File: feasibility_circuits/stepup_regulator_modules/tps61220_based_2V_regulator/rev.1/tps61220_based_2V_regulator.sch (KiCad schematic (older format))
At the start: 19 parts

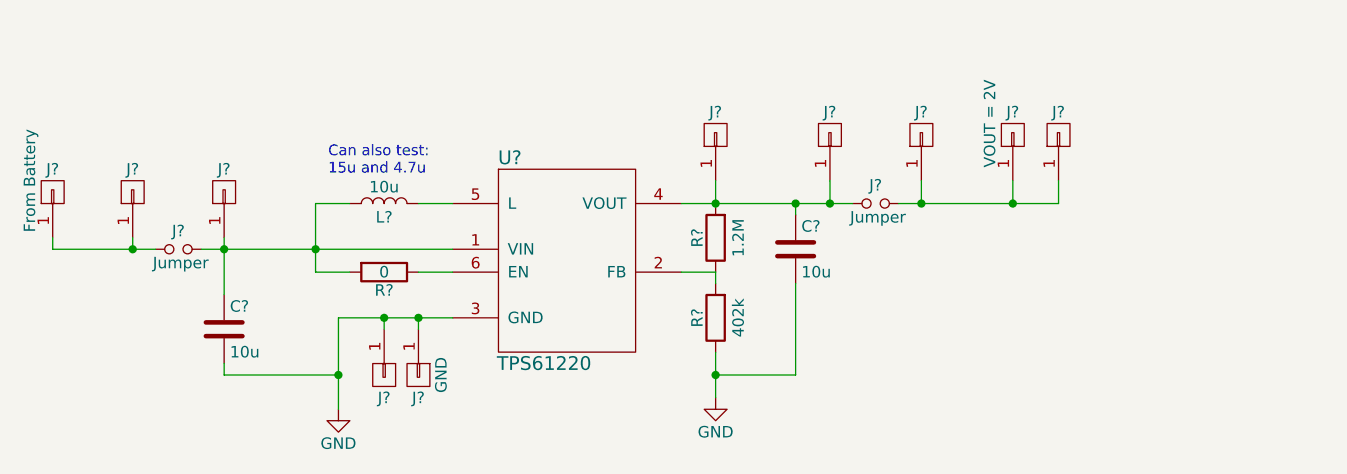
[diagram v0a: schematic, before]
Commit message: Finished layout of the TPS61220 regulator board
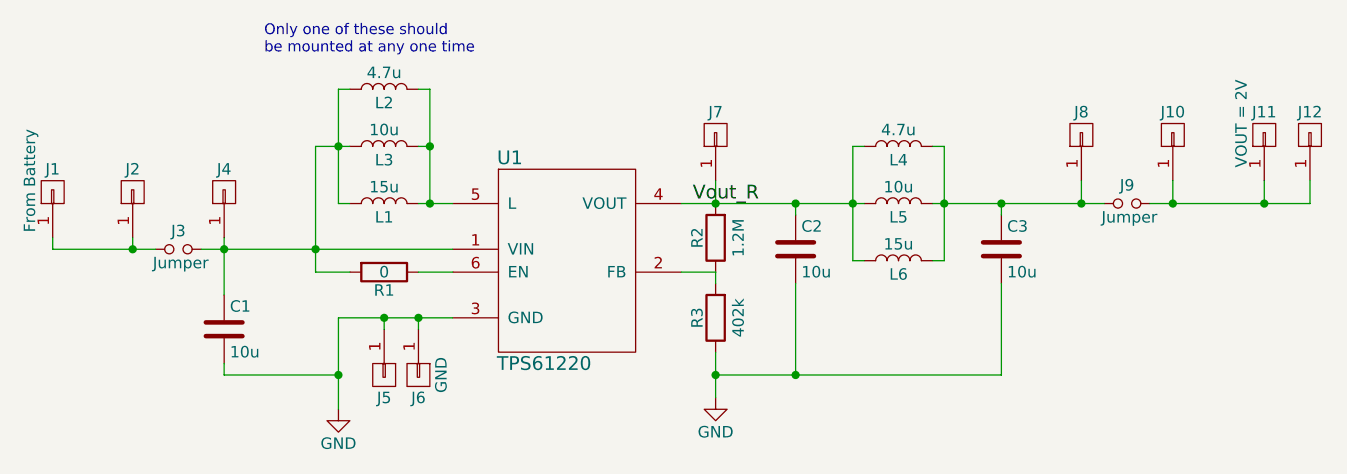
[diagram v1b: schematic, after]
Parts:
- added C3: 10u, Capacitors_SMD:C_0805_HandSoldering, symbol C
- added L2, L4: 4.7u, Custom SMD Inductors:proto_inductor-smd_0805, symbol L
- added L3, L5: 10u, Custom SMD Inductors:proto_inductor-smd_1008, symbol L
- added L6: 15u, Custom SMD Inductors:proto_inductor-smd_1210, symbol L
- C1, C2: renamed from C?; footprint (none) -> Capacitors_SMD:C_0805_HandSoldering
- J3, J9: renamed from J?; footprint (none) -> Custom SMD Connectors:proto_header-vt-1x2-2.54mm-G_C__SABN_M30
- L1: renamed from L?; value 10u -> 15u; footprint (none) -> Custom SMD Inductors:proto_inductor-smd_1210
- R1, R2, R3: renamed from R?; footprint (none) -> Resistors_SMD:R_0805_HandSoldering
- U1: renamed from U?; footprint (none) -> Custom SMD Amplifiers:proto_amp-ti_tps6122
- gave numbers to parts that had none: 10
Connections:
- net GND: now also C3.2
- net at C1.1, J3.2, J4.1 (P1)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: now also L2.1, L3.1
- net at L1.2, U1.5 (L): now also L2.2, L3.2
- net Vout_R: now reaches C2.1, J7.1 (P1), R2.2, U1.4 (VOUT)
- net Vout_R: now also L4.1, L5.1, L6.1; no longer J8.1 (P1), J9.1
- new net: C3.1, J8.1 (P1), J9.1, L4.2, L5.2, L6.2
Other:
- note added: "Only one of these should \nbe mounted at any one time"
- note removed: "Can also test:\n15u and 4.7u"
- moved on the sheet: J10, J11, J12, J8, J9
